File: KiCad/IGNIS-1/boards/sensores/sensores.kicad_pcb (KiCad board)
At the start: 2 copper layers, 62 x 62 mm, 15 parts, among them J41 Backplane_2x10, U20 BME280, U21 MPU6050, U22 MQ-135, U24 GPS NEO-6M

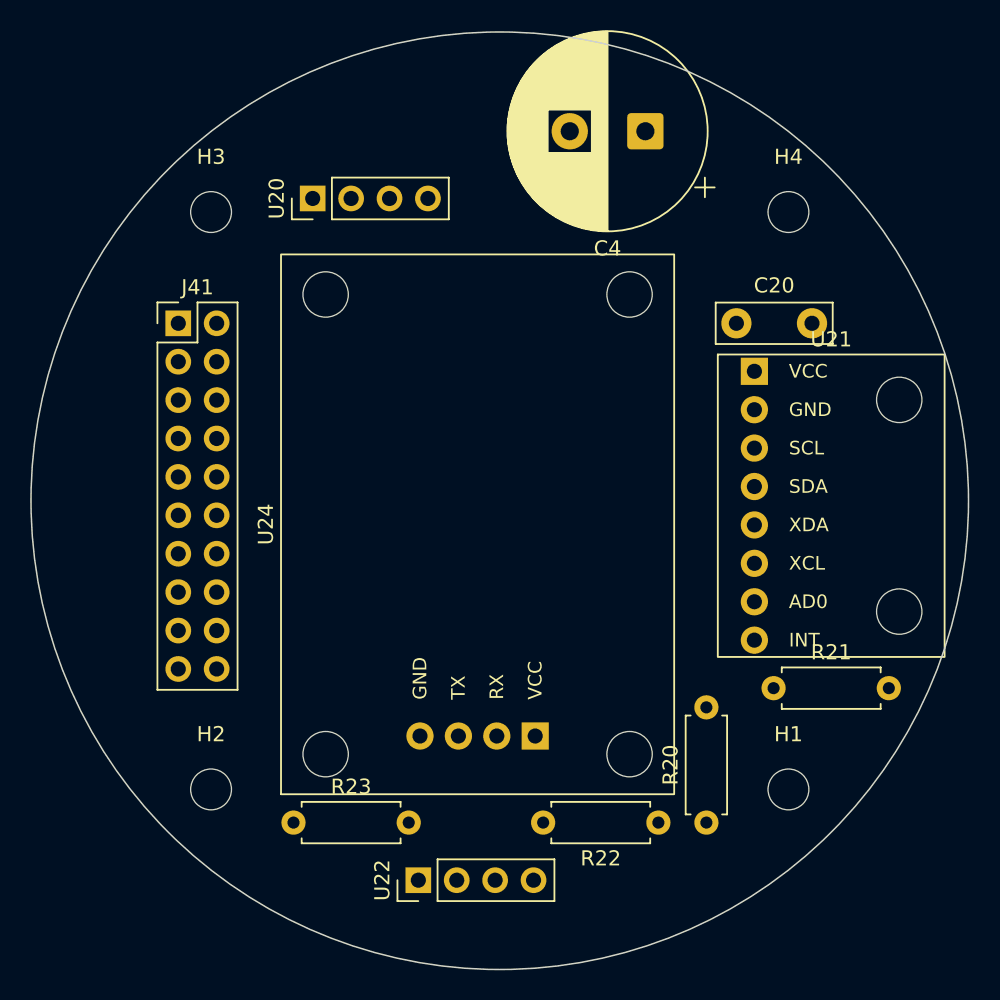
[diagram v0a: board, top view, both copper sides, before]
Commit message: 5 boards separados, falta ajustar dimensiones de BME280 y MQ-135
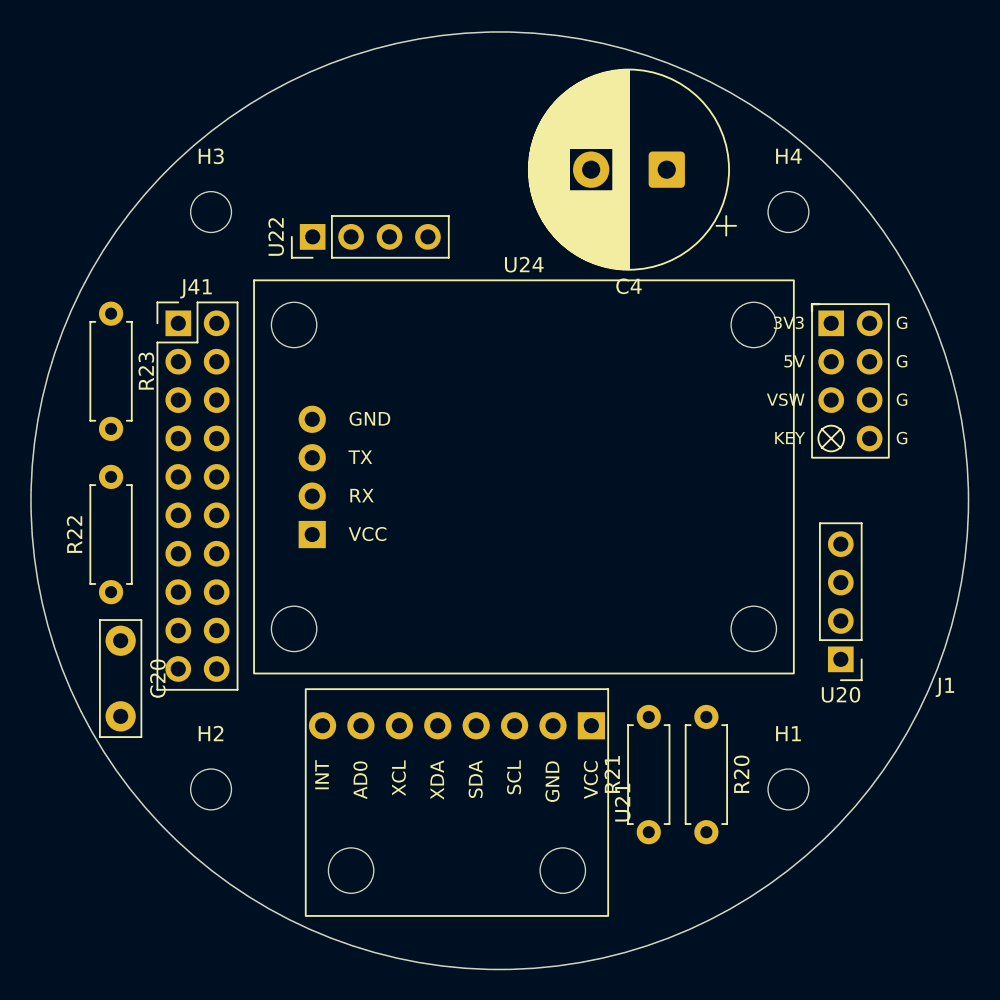
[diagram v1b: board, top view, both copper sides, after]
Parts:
- added J1: J_PWR_2x4, IGNIS1:J_PWR_2x4_Keyed, F.Cu at (123.2, 92.1)
- J41: value Backplane_2x10 -> J_DAT
- moved U20 46.4 mm to (122.6, 110.5), turned to 180 degrees
- moved C20 45.8 mm to (74.9, 109.3), turned to -90 degrees
- moved U22 43.1 mm to (87.6, 82.5)
- moved R22 39.3 mm to (74.3, 106.0), turned to 90 degrees
- moved R23 35.8 mm to (74.3, 87.6), turned to -90 degrees
- moved U21 31.6 mm to (97.2, 120.0), turned to -90 degrees
- moved R21 12.6 mm to (109.9, 121.9), turned to 90 degrees
- moved R20 6.98 mm to (113.7, 114.3), turned to -90 degrees
- moved U24 4.38 mm to (101.6, 98.4), turned to 0 degrees
- moved C4 2.91 mm to (111.0, 78.1)
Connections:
- J41 pad 1: +3V3 -> unconnected-(J41-Pin_1-Pad1)
- J41 pad 19: +5V -> unconnected-(J41-Pin_19-Pad19)
- R20 pad 1: SDA -> +3V3
- R20 pad 2: +3V3 -> SDA
- R21 pad 1: SCL -> +3V3
- R21 pad 2: +3V3 -> SCL

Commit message: Se agregaron tracks. PCB Cerebro libre de errores.
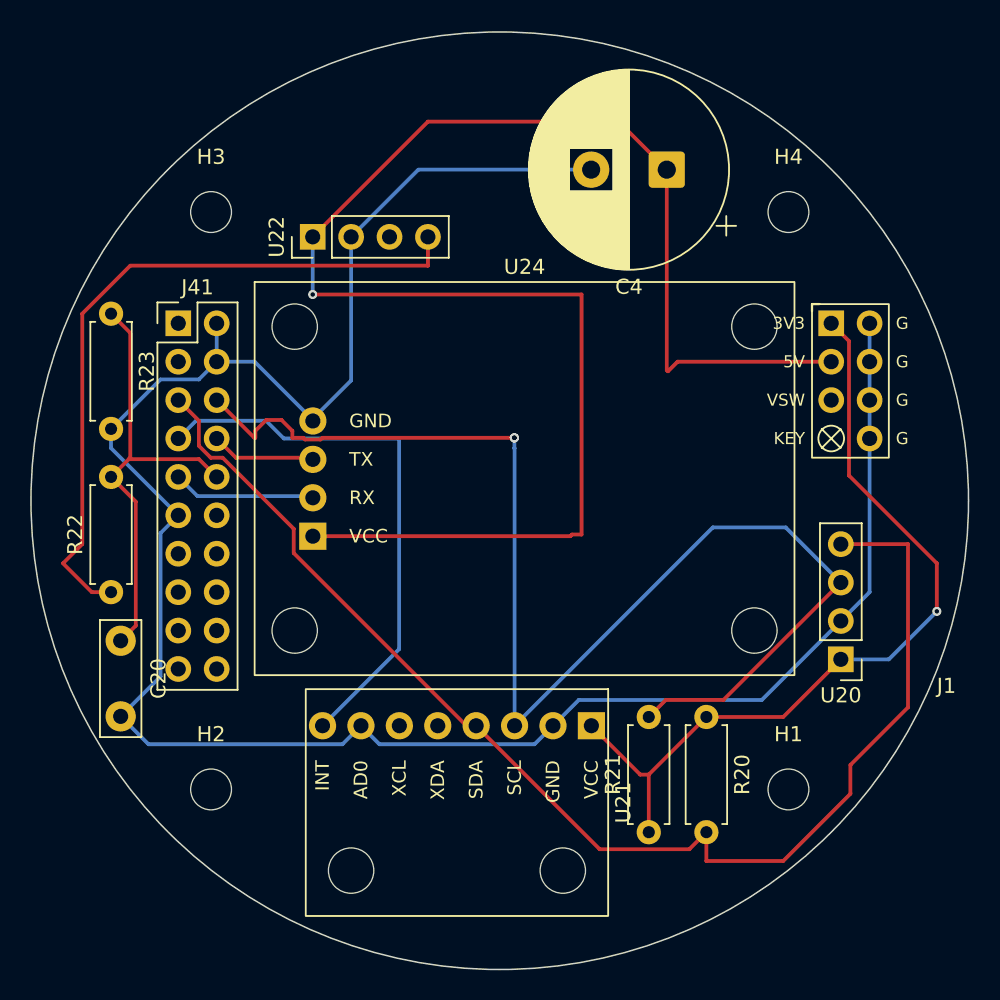
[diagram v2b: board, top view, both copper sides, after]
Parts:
- moved U24 0.12 mm to (101.6, 98.5)
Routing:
- net GND: track 0.00 -> 145.8 mm
- net +5V: track 0.00 -> 107.6 mm, vias 0 -> 1
- net SCL: track 0.00 -> 86.3 mm, vias 0 -> 2
- net SDA: track 0.00 -> 84.8 mm
- net +3V3: track 0.00 -> 54.4 mm, vias 0 -> 1
- net Net-(U22-A0): track 0.00 -> 47.1 mm
- net MPU_INT: track 0.00 -> 36.7 mm
- net MQ_AOUT: track 0.00 -> 30.1 mm
- net GPS_RX: track 0.00 -> 9.39 mm
- net GPS_TX: track 0.00 -> 6.85 mm

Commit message: Todos los boards pasan el check, tracks completos
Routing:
- net MPU_INT: track 36.7 -> 25.9 mm
- net SCL: track 86.3 -> 75.7 mm, vias 2 -> 1
- net +5V: track 107.6 -> 105.5 mm
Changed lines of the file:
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@@
 		(tags "Resistor Axial_DIN0207 series Axial Horizontal pin pitch 7.62mm 0.25W = 1/4W length 6.3mm diameter 2.5mm")
 		(property "Reference" "R21"
-			(at 3.81 -2.37 90)
+			(at 3.81 0 90)
 			(layer "F.SilkS")
 			(effects
@@
 		(descr "MPU6050 GY-521 module 15x20mm - 8 THT pins 1-row P2.54 on left, 2x M3 mounting holes right. Module mounts face-up, pins down (mezzanine). Top view 1:1, no mirror. Pad1=VCC top ... Pad8=INT bottom.")
 		(property "Reference" "U21"
-			(at 0 -11 90)
+			(at 6.278 -11.161 90)
 			(layer "F.SilkS")
 			(effects
@@
 		(tags "Resistor Axial_DIN0207 series Axial Horizontal pin pitch 7.62mm 0.25W = 1/4W length 6.3mm diameter 2.5mm")
 		(property "Reference" "R22"
-			(at 3.81 -2.37 90)
+			(at 3.81 0 90)
 			(layer "F.SilkS")
 			(effects
@@
 		(tags "Resistor Axial_DIN0207 series Axial Horizontal pin pitch 7.62mm 0.25W = 1/4W length 6.3mm diameter 2.5mm")
 		(property "Reference" "R23"
-			(at 3.81 -2.37 90)
+			(at 3.81 0 90)
 			(layer "F.SilkS")
 			(effects
@@
 		(tags "Resistor Axial_DIN0207 series Axial Horizontal pin pitch 7.62mm 0.25W = 1/4W length 6.3mm diameter 2.5mm")
 		(property "Reference" "R20"
-			(at 3.81 -2.37 90)
+			(at 3.81 0 90)
 			(layer "F.SilkS")
 			(effects
@@
 			(at 2.5 -7.75 0)
 			(layer "F.SilkS")
+			(hide yes)
 			(effects
 				(font
@@
 			(layer "F.CrtYd")
 		)
-		(fp_text user "3V3"
-			(at -3 -3.81 0)
+		(fp_text user ""
+			(at -3 1.27 0)
 			(layer "F.SilkS")
 			(effects
@@
 			)
 		)
-		(fp_text user "5V"
-			(at -3 -1.27 0)
+		(fp_text user ""
+			(at -3 3.81 0)
 			(layer "F.SilkS")
 			(effects
@@
 			)
 		)
-		(fp_text user "VSW"
-			(at -3 1.27 0)
+		(fp_text user "3V3"
+			(at -0.635 -5.969 0)
 			(layer "F.SilkS")
 			(effects
@@
 			)
 		)
-		(fp_text user "KEY"
-			(at -3 3.81 0)
+		(fp_text user "5V"
+			(at 0.635 -2.3114 0)
 			(layer "F.SilkS")
 			(effects
@@
 		(tags "C Disc series Radial pin pitch 5.00mm diameter 7.5mm width 2.5mm Capacitor")
 		(property "Reference" "C20"
-			(at 2.5 -2.5 90)
+			(at 2.5 0 90)
 			(layer "F.SilkS")
 			(effects
@@
 	)
 	(segment
-		(start 122.555 105.41)
-		(end 114.79 113.175)
-		(width 0.25)
-		(layer "F.Cu")
-		(net "SCL")
-	)
-	(segment
-		(start 87.022588 95.84)
-		(end 86.285 95.84)
-		(width 0.25)
-		(layer "F.Cu")
-		(net "SCL")
-	)
-	(segment
-		(start 114.79 113.175)
-		(end 110.98 113.175)
+		(start 88.147412 95.95)
+		(end 83.885 95.95)
 		(width 0.25)
 		(layer "F.Cu")
@@
 	)
 	(segment
-		(start 84.552588 94.66)
-		(end 83.835 95.377588)
+		(start 100.98 99.8474)
+		(end 96.9726 95.84)
 		(width 0.25)
 		(layer "F.Cu")
@@
 	)
 	(segment
-		(start 100.965 95.84)
-		(end 100.98 95.84)
+		(start 96.9726 95.84)
+		(end 88.257412 95.84)
 		(width 0.25)
 		(layer "F.Cu")
@@
 	)
 	(segment
-		(start 86.285 95.377588)
-		(end 85.567412 94.66)
-		(width 0.25)
-		(layer "F.Cu")
-		(net "SCL")
-	)
-	(segment
-		(start 110.98 113.175)
+		(start 109.21 113.655)
 		(end 109.855 114.3)
 		(width 0.25)
@@
 	)
 	(segment
-		(start 100.965 95.84)
-		(end 88.257412 95.84)
-		(width 0.25)
-		(layer "F.Cu")
-		(net "SCL")
-	)
-	(segment
-		(start 86.285 95.84)
-		(end 86.285 95.377588)
+		(start 102.205 113.655)
+		(end 109.21 113.655)
 		(width 0.25)
 		(layer "F.Cu")
@@
 	)
 	(segment
-		(start 83.775 95.84)
+		(start 83.885 95.95)
 		(end 81.28 93.345)
 		(width 0.25)
@@
 	)
 	(segment
-		(start 83.835 95.84)
-		(end 83.775 95.84)
-		(width 0.25)
-		(layer "F.Cu")
-		(net "SCL")
-	)
-	(segment
-		(start 83.835 95.377588)
-		(end 83.835 95.84)
-		(width 0.25)
-		(layer "F.Cu")
-		(net "SCL")
-	)
-	(segment
-		(start 87.132588 95.95)
-		(end 87.022588 95.84)
-		(width 0.25)
-		(layer "F.Cu")
-		(net "SCL")
-	)
-	(segment
-		(start 85.567412 94.66)
-		(end 84.552588 94.66)
-		(width 0.25)
-		(layer "F.Cu")
-		(net "SCL")
-	)
-	(segment
-		(start 88.147412 95.95)
-		(end 87.132588 95.95)
+		(start 100.98 114.88)
+		(end 102.205 113.655)
 		(width 0.25)
 		(layer "F.Cu")
@@
 	)
 	(via
-		(at 100.965 95.84)
-		(size 0.6)
-		(drill 0.3)
-		(layers "F.Cu" "B.Cu")
-		(net "SCL")
-	)
-	(via
-		(at 100.965 95.84)
+		(at 100.98 99.8474)
 		(size 0.6)
 		(drill 0.3)
@@
 	)
 	(segment
-		(start 100.965 96.52)
-		(end 100.98 96.535)
-		(width 0.25)
-		(layer "B.Cu")
-		(net "SCL")
-	)
-	(segment
-		(start 100.965 95.84)
-		(end 100.965 96.52)
+		(start 100.98 99.8474)
+		(end 100.98 114.88)
 		(width 0.25)
 		(layer "B.Cu")
@@
 	)
 	(segment
-		(start 100.98 96.535)
-		(end 100.98 114.88)
-		(width 0.25)
-		(layer "B.Cu")
-		(net "SCL")
-	)
-	(segment
 		(start 124.46 93.345)
 		(end 124.46 90.805)
@@
 	)
 	(segment
-		(start 85.725 95.885)
-		(end 93.345 95.885)
+		(start 77.565 98.911701)
+		(end 77.565 97.06)
+		(width 0.25)
+		(layer "B.Cu")
+		(net "MPU_INT")
+	)
+	(segment
+		(start 80.105 100.478299)
+		(end 79.226701 99.6)
+		(width 0.25)
+		(layer "B.Cu")
+		(net "MPU_INT")
+	)
+	(segment
+		(start 79.226701 99.6)
+		(end 78.253299 99.6)
+		(width 0.25)
+		(layer "B.Cu")
+		(net "MPU_INT")
+	)
+	(segment
+		(start 88.28 114.88)
+		(end 83.16 109.76)
 		(width 0.25)
 		(layer "B.Cu")
@@
 	)
 	(segment
-		(start 93.345 109.815)
-		(end 88.28 114.88)
+		(start 83.16 109.76)
+		(end 80.793299 109.76)
 		(width 0.25)
 		(layer "B.Cu")
@@
 	)
 	(segment
-		(start 78.74 95.885)
-		(end 79.915 94.71)
+		(start 77.565 97.06)
+		(end 78.74 95.885)
 		(width 0.25)
 		(layer "B.Cu")
@@
 	)
 	(segment
-		(start 93.345 95.885)
-		(end 93.345 109.815)
+		(start 80.793299 109.76)
+		(end 80.105 109.071701)
 		(width 0.25)
 		(layer "B.Cu")
@@
 	)
 	(segment
-		(start 79.915 94.71)
-		(end 84.55 94.71)
+		(start 80.105 109.071701)
+		(end 80.105 100.478299)
 		(width 0.25)
 		(layer "B.Cu")
@@
 	)
 	(segment
-		(start 84.55 94.71)
-		(end 85.725 95.885)
+		(start 78.253299 99.6)
+		(end 77.565 98.911701)
 		(width 0.25)
 		(layer "B.Cu")
@@
 	)
 	(segment
-		(start 111.045 91.36)
-		(end 111.125 91.44)
-		(width 0.25)
-		(layer "F.Cu")
-		(net "+5V")
-	)
-	(segment
 		(start 104.665 102.345)
 		(end 87.64 102.345)
@@
 	)
 	(segment
-		(start 111.125 91.44)
-		(end 111.76 90.805)
+		(start 113.1062 90.805)
+		(end 111.045 88.7438)
 		(width 0.25)
 		(layer "F.Cu")
@@
 	(segment
 		(start 111.045 78.105)
-		(end 111.045 91.36)
+		(end 111.045 88.7438)
 		(width 0.25)
 		(layer "F.Cu")
@@
 	)
 	(segment
-		(start 111.76 90.805)
+		(start 113.1062 90.805)
 		(end 121.92 90.805)
 		(width 0.25)

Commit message: Actualización archivos KiCad
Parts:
- moved U20 8.00 mm to (123.0, 102.5), turned to 0 degrees
- moved U22 7.87 mm to (95.5, 82.5), turned to -90 degrees
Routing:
- net +5V: track 105.5 -> 90.4 mm, vias 1 -> 0
- net SDA: track 84.8 -> 71.4 mm
- net Net-(U22-A0): track 47.1 -> 38.6 mm
- net +3V3: track 54.4 -> 47.7 mm, vias 1 -> 0
- net GND: track 145.8 -> 149.1 mm
- net SCL: track 75.7 -> 78.0 mm
